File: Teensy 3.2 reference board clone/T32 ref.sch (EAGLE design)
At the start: 89 parts, among them K1 MK20DX256VLH7, K2 MKL04Z32VLC4, P1 LED, T1 MCP1825S - 3.3V, X1 MINI-USB

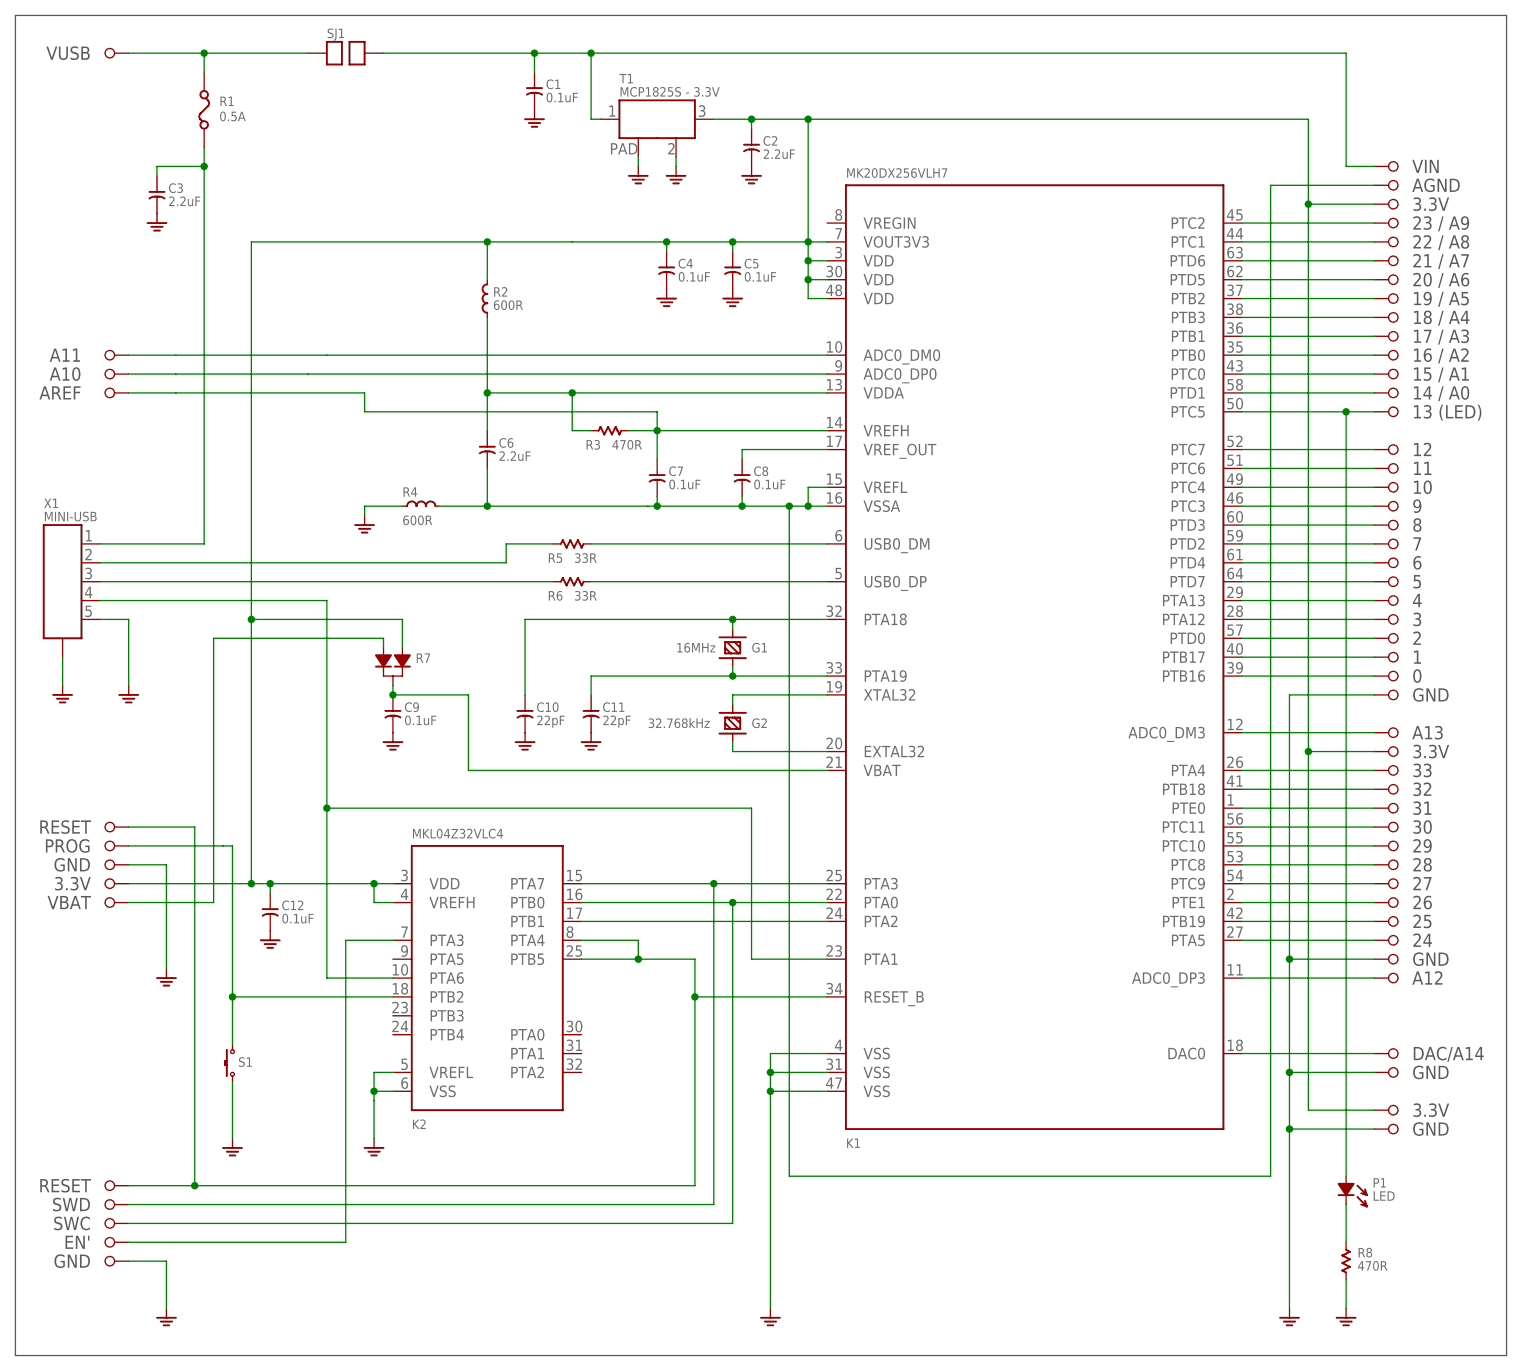
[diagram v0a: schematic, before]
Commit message: change led and switch, add gerber files for osh park
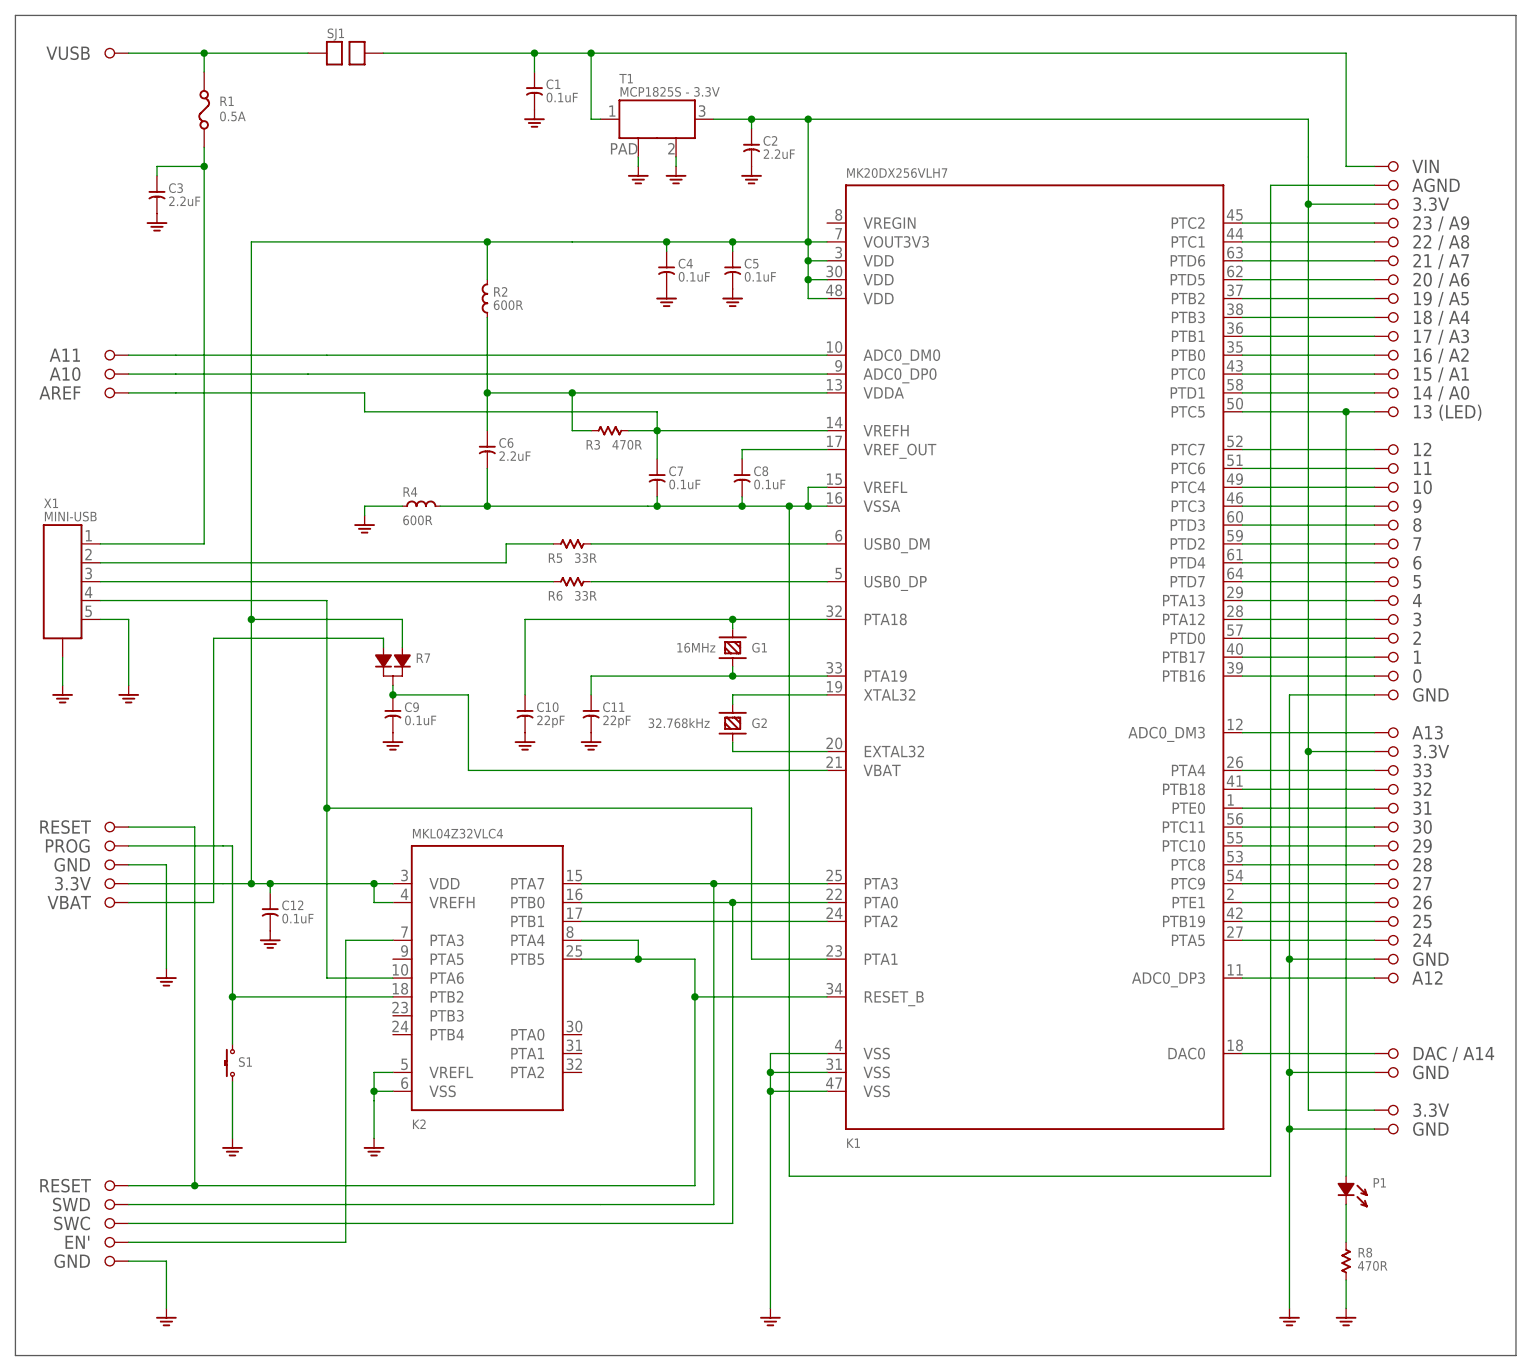
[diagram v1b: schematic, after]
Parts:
- P1: value LED -> (none)
- S1: device t32_ref:SWITCH -> t32_ref:TACT_SWITCH
- X1: MF Hirose -> (none); MPN UX60-MB-5ST -> (none)
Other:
- note added: "DAC / A14"
- note removed: "DAC/A14"
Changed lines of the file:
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@@
 <part name="GND8" library="t32_ref" deviceset="GND" device=""/>
 <part name="X1" library="t32_ref" deviceset="MINI-USB" device="UX60-MB-5ST" value="MINI-USB">
-<attribute name="MF" value="Hirose"/>
-<attribute name="MPN" value="UX60-MB-5ST"/>
 <attribute name="OC_MOUSER" value="798-UX60-MB-5ST"/>
 </part>
@@
 <part name="GND2" library="t32_ref" deviceset="GND" device=""/>
 <part name="R7" library="t32_ref" deviceset="DIODE_DUAL" device=""/>
-<part name="P1" library="t32_ref" deviceset="LED" device="" value="LED"/>
+<part name="P1" library="t32_ref" deviceset="LED" device=""/>
 <part name="GND21" library="t32_ref" deviceset="GND" device=""/>
 <part name="GND15" library="t32_ref" deviceset="GND" device=""/>
-<part name="S1" library="t32_ref" deviceset="SWITCH" device=""/>
+<part name="S1" library="t32_ref" deviceset="TACT_SWITCH" device=""/>
 <part name="GND16" library="t32_ref" deviceset="GND" device=""/>
 <part name="SJ1" library="t32_ref" deviceset="SOLDERJUMPER" device=""/>
@@
 <text x="187.96" y="53.34" size="1.778" layer="97" align="center-left">GND</text>
 <text x="187.96" y="50.8" size="1.778" layer="97" align="center-left">A12</text>
-<text x="187.96" y="40.64" size="1.778" layer="97" align="center-left">DAC/A14</text>
+<text x="187.96" y="40.64" size="1.778" layer="97" align="center-left">DAC / A14</text>
 <text x="10.16" y="66.04" size="1.778" layer="97" rot="R180" align="center-left">GND</text>
 <text x="10.16" y="60.96" size="1.778" layer="97" rot="R180" align="center-left">VBAT</text>
@@
 <text x="187.96" y="38.1" size="1.778" layer="97" align="center-left">GND</text>
 <text x="187.96" y="33.02" size="1.778" layer="97" align="center-left">3.3V</text>
-<wire x1="0" y1="180.34" x2="200.66" y2="180.34" width="0.1524" layer="97"/>
-<wire x1="200.66" y1="180.34" x2="200.66" y2="0" width="0.1524" layer="97"/>
-<wire x1="200.66" y1="0" x2="0" y2="0" width="0.1524" layer="97"/>
+<wire x1="0" y1="180.34" x2="201.93" y2="180.34" width="0.1524" layer="97"/>
+<wire x1="201.93" y1="180.34" x2="201.93" y2="0" width="0.1524" layer="97"/>
+<wire x1="201.93" y1="0" x2="0" y2="0" width="0.1524" layer="97"/>
 <wire x1="0" y1="0" x2="0" y2="180.34" width="0.1524" layer="97"/>
 </plain>

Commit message: change usb mini from Hirose to Molex
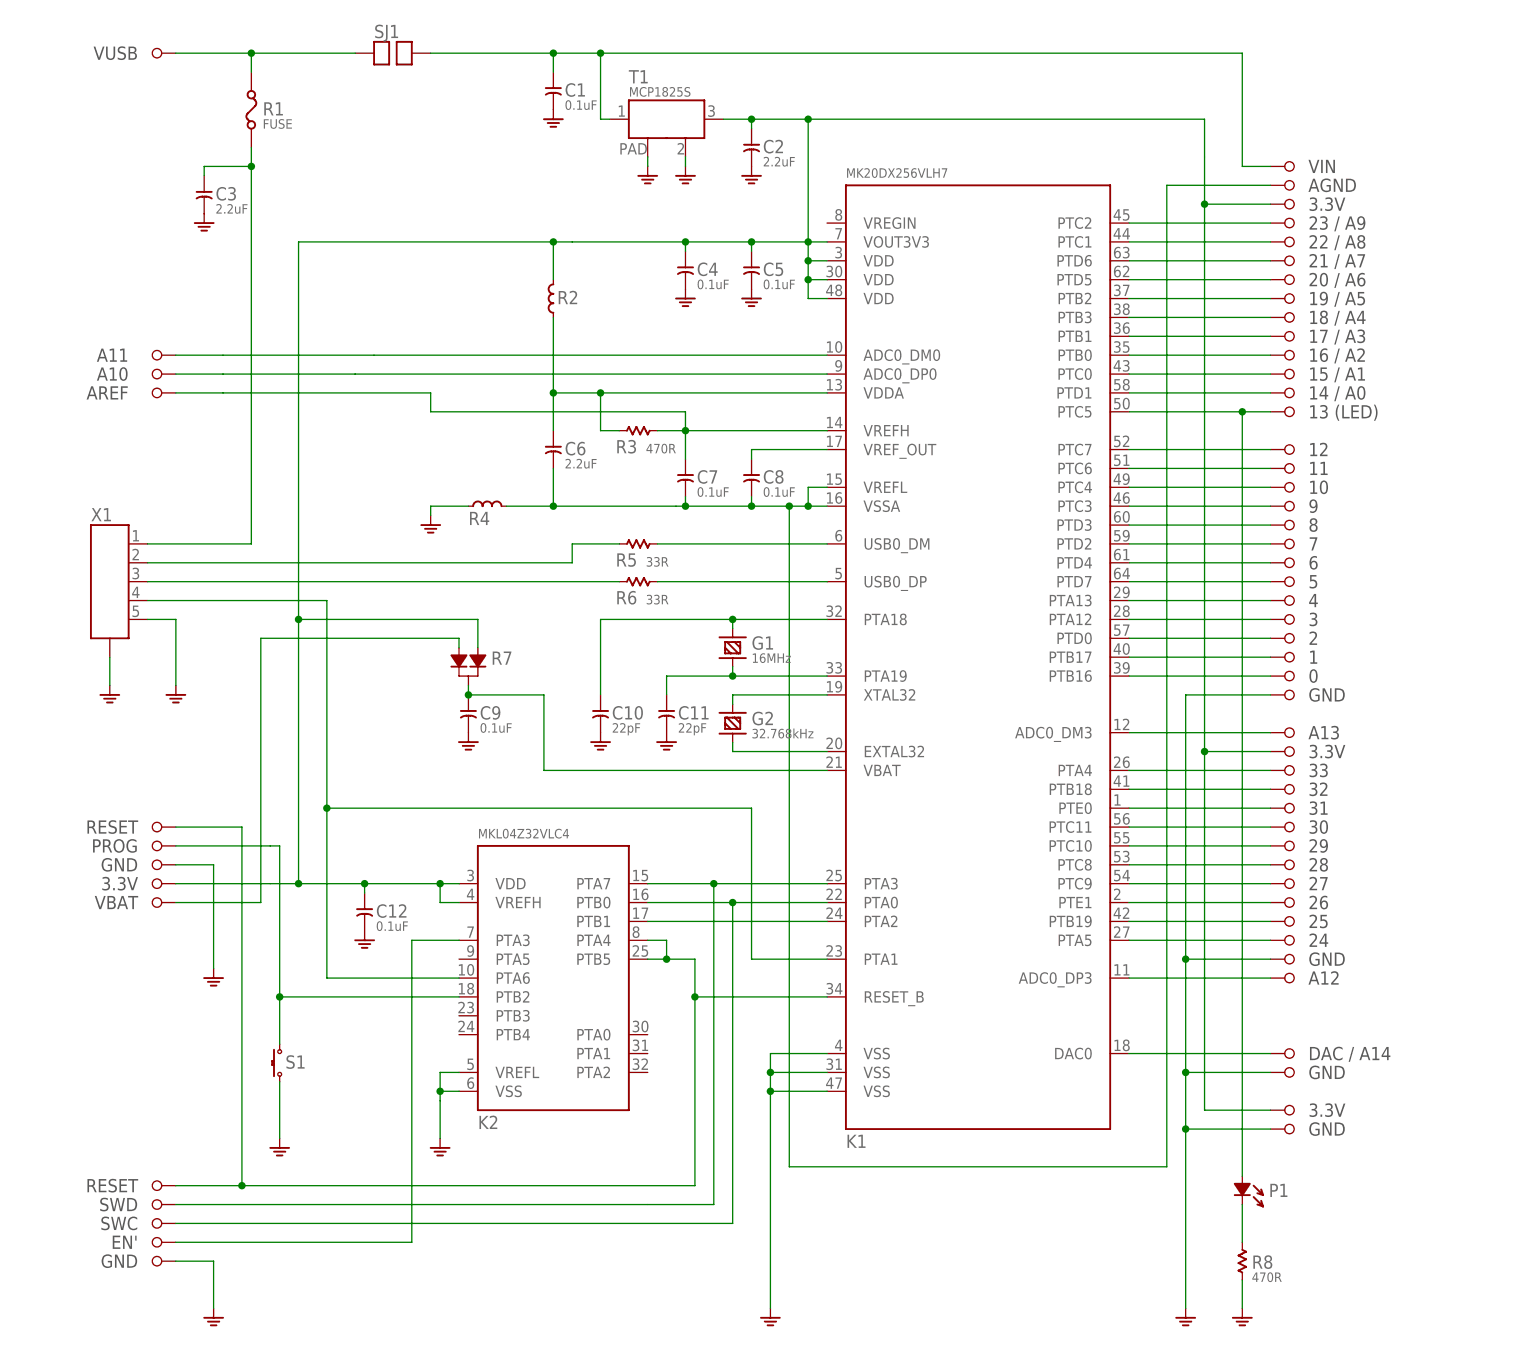
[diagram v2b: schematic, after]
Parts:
- R1: value 0.5A -> FUSE
- R2, R4: value 600R -> (none)
- T1: value MCP1825S - 3.3V -> MCP1825S
- X1: device t32_ref:MINI-USBUX60-MB-5ST -> t32_ref:MINI-USBMOLEX_0675031230; OC_MOUSER 798-UX60-MB-5ST -> (none)
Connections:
- net N$63: now also R7.2; no longer R7.1
- net N$69: now also R7.1; no longer R7.2
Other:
- moved on the sheet: C1, C10, C11, C12, C3, C4, C5, C6, C7, C8, C9, K1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
